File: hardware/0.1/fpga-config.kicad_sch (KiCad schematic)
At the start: 37 parts, among them J2 JTAG, J5 USB_C_Receptacle_USB2.0, Q1 BSS138, SW1 SW_Push, U1 ECP5U_12_CABGA256, U4 USBLC6-2SC6, U6 W25Q128JVSIQ

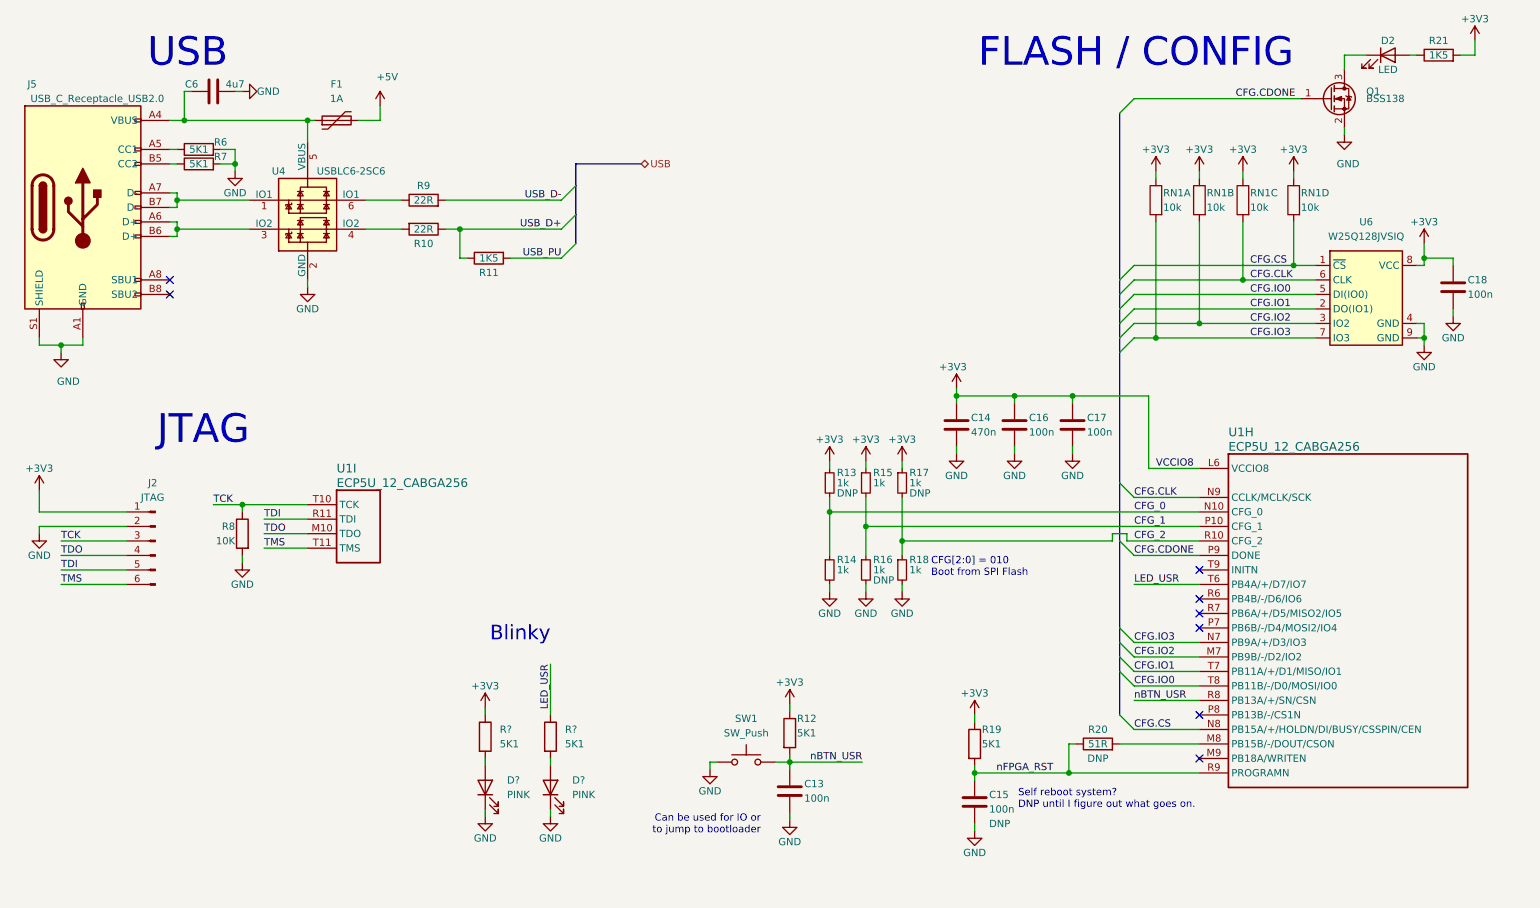
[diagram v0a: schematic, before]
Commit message: all 3d models added
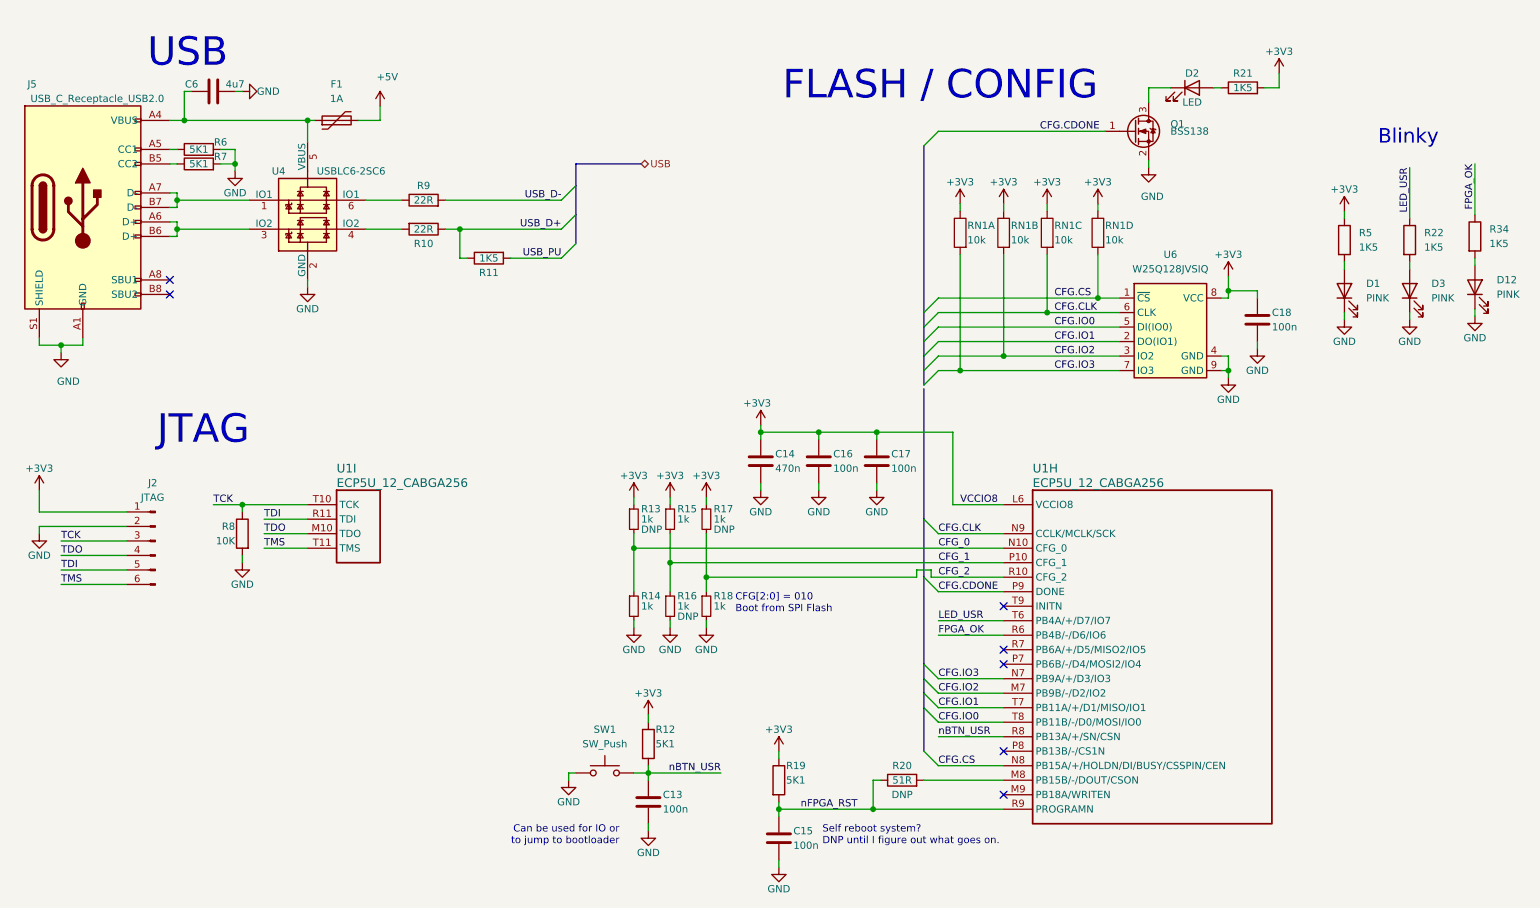
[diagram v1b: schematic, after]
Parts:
- added D12: PINK, LED_SMD:LED_0603_1608Metric, symbol Device:LED
- added R34: 1K5, Resistor_SMD:R_0402_1005Metric, symbol Device:R
- C15: DNP DNP -> (none)
- F1: footprint josh-passives-smt:Fuse_0805_2012Metric -> josh-passives-smt:Fuse_0603_1608Metric
- Q1: footprint Package_TO_SOT_SMD:SOT-23 -> Package_TO_SOT_SMD:SOT-323_SC-70
- R22, R5: renamed from R?; value 5K1 -> 1K5
- SW1: footprint josh-buttons-switches:SW_Push_PTS815 -> josh-buttons-switches:SW_Push_KMR2
- U6: footprint Package_SON:WSON-8-1EP_6x5mm_P1.27mm_EP3.4x4.3mm -> josh-soic-sot-etc:WSON-8-1EP_6x5mm_P1.27mm_EP3.4x4.3mm
- gave numbers to parts that had none: 2
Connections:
- net GND: now also D12.1 (K)
- net FPGA_OK: now reaches U1.R6 (PB4B/-/D6/IO6)
- net FPGA_OK: now also R34.1
- new net: D12.2 (A), R34.2
- no-connect marks 8 -> 7
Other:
- moved on the sheet: C13, C14, C15, C16, C17, C18, D1, D2, D3, Q1, R12, R13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

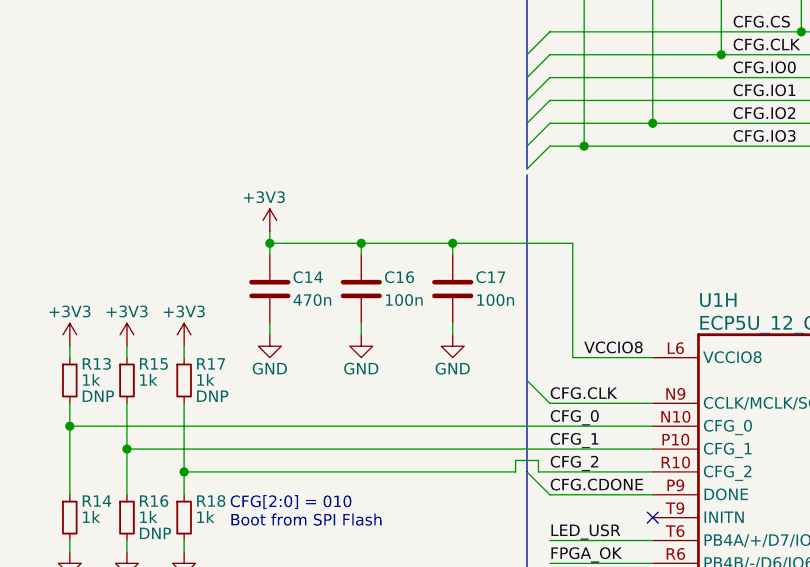
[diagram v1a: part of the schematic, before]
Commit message: decoupling down + outer pins fanned out
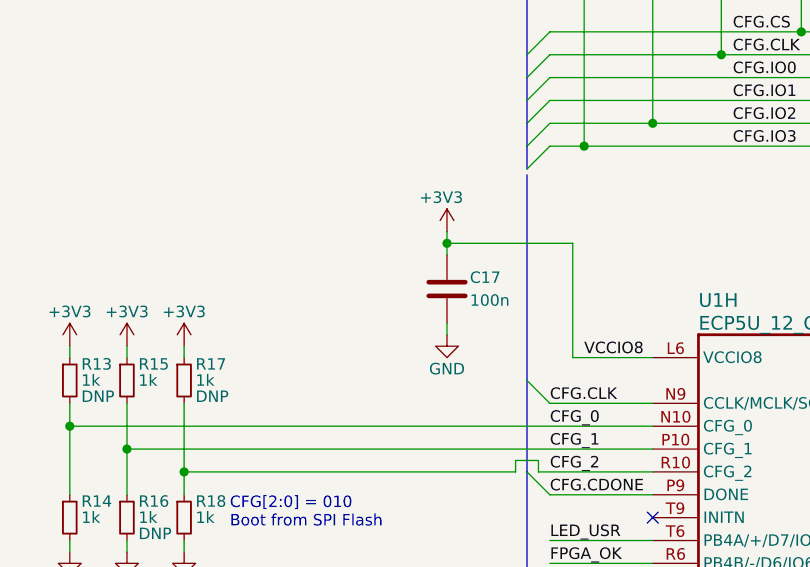
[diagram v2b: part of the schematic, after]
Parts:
- removed C14: 470n, Capacitor_SMD:C_0402_1005Metric, symbol Device:C
- removed C16: 100n, Capacitor_SMD:C_0402_1005Metric, symbol Device:C
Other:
- moved on the sheet: C17
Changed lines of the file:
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@@
   (junction (at 134.62 110.49) (diameter 1.016) (color 0 0 0 0))
   (junction (at 140.97 113.03) (diameter 1.016) (color 0 0 0 0))
-  (junction (at 150.495 87.63) (diameter 1.016) (color 0 0 0 0))
   (junction (at 153.67 153.67) (diameter 1.016) (color 0 0 0 0))
-  (junction (at 160.655 87.63) (diameter 1.016) (color 0 0 0 0))
+  (junction (at 170.18 87.63) (diameter 1.016) (color 0 0 0 0))
   (junction (at 170.18 153.67) (diameter 1.016) (color 0 0 0 0))
-  (junction (at 170.815 87.63) (diameter 1.016) (color 0 0 0 0))
   (junction (at 185.42 76.835) (diameter 1.016) (color 0 0 0 0))
   (junction (at 193.04 74.295) (diameter 1.016) (color 0 0 0 0))
@@
   (junction (at 232.41 62.865) (diameter 1.016) (color 0 0 0 0))
   (junction (at 232.41 76.835) (diameter 1.016) (color 0 0 0 0))
-  (no_connect (at 46.99 60.96))
-  (no_connect (at 193.04 143.51))
-  (no_connect (at 193.04 118.11))
-  (no_connect (at 46.99 63.5))
   (no_connect (at 193.04 125.73))
   (no_connect (at 193.04 128.27))
   (no_connect (at 193.04 151.13))
+  (no_connect (at 46.99 63.5))
+  (no_connect (at 193.04 118.11))
+  (no_connect (at 193.04 143.51))
+  (no_connect (at 46.99 60.96))
   (bus_entry (at 115.57 46.99) (size 2.54 -2.54)
     (stroke (width 0.1524) (type solid) (color 0 0 0 0))
@@
     (stroke (width 0) (type solid) (color 0 0 0 0))
   )
-  (wire (pts (xy 150.495 86.36) (xy 150.495 87.63))
-    (stroke (width 0) (type solid) (color 0 0 0 0))
-  )
-  (wire (pts (xy 150.495 87.63) (xy 150.495 88.9))
-    (stroke (width 0) (type solid) (color 0 0 0 0))
-  )
-  (wire (pts (xy 150.495 96.52) (xy 150.495 97.79))
-    (stroke (width 0) (type solid) (color 0 0 0 0))
-  )
   (wire (pts (xy 153.67 143.51) (xy 153.67 144.78))
     (stroke (width 0) (type solid) (color 0 0 0 0))
@@
     (stroke (width 0) (type solid) (color 0 0 0 0))
   )
-  (wire (pts (xy 160.655 87.63) (xy 150.495 87.63))
-    (stroke (width 0) (type solid) (color 0 0 0 0))
-  )
-  (wire (pts (xy 160.655 87.63) (xy 160.655 88.9))
-    (stroke (width 0) (type solid) (color 0 0 0 0))
-  )
-  (wire (pts (xy 160.655 87.63) (xy 170.815 87.63))
-    (stroke (width 0) (type solid) (color 0 0 0 0))
-  )
-  (wire (pts (xy 160.655 96.52) (xy 160.655 97.79))
+  (wire (pts (xy 170.18 86.36) (xy 170.18 87.63))
+    (stroke (width 0) (type solid) (color 0 0 0 0))
+  )
+  (wire (pts (xy 170.18 87.63) (xy 170.18 88.9))
+    (stroke (width 0) (type solid) (color 0 0 0 0))
+  )
+  (wire (pts (xy 170.18 87.63) (xy 184.15 87.63))
+    (stroke (width 0) (type solid) (color 0 0 0 0))
+  )
+  (wire (pts (xy 170.18 96.52) (xy 170.18 97.79))
     (stroke (width 0) (type solid) (color 0 0 0 0))
   )
@@
   )
   (wire (pts (xy 170.18 153.67) (xy 193.04 153.67))
-    (stroke (width 0) (type solid) (color 0 0 0 0))
-  )
-  (wire (pts (xy 170.815 87.63) (xy 170.815 88.9))
-    (stroke (width 0) (type solid) (color 0 0 0 0))
-  )
-  (wire (pts (xy 170.815 87.63) (xy 184.15 87.63))
-    (stroke (width 0) (type solid) (color 0 0 0 0))
-  )
-  (wire (pts (xy 170.815 96.52) (xy 170.815 97.79))
     (stroke (width 0) (type solid) (color 0 0 0 0))
   )
@@
     )
   )
-  (symbol (lib_id "power:+3V3") (at 150.495 86.36 0) (unit 1)
-    (in_bom yes) (on_board yes)
-    (property "Reference" "#PWR0141" (id 0) (at 150.495 90.17 0)
-      (effects (font (size 1.27 1.27)) hide)
-    )
-    (property "Value" "+3V3" (id 1) (at 149.86 82.55 0))
-    (property "Footprint" "" (id 2) (at 150.495 86.36 0)
-      (effects (font (size 1.27 1.27)) hide)
-    )
-    (property "Datasheet" "" (id 3) (at 150.495 86.36 0)
-      (effects (font (size 1.27 1.27)) hide)
-    )
-  )
   (symbol (lib_id "power:+3V3") (at 153.67 143.51 0) (unit 1)
     (in_bom yes) (on_board yes)
@@
     )
   )
+  (symbol (lib_id "power:+3V3") (at 170.18 86.36 0) (unit 1)
+    (in_bom yes) (on_board yes)
+    (property "Reference" "#PWR0141" (id 0) (at 170.18 90.17 0)
+      (effects (font (size 1.27 1.27)) hide)
+    )
+    (property "Value" "+3V3" (id 1) (at 169.545 82.55 0))
+    (property "Footprint" "" (id 2) (at 170.18 86.36 0)
+      (effects (font (size 1.27 1.27)) hide)
+    )
+    (property "Datasheet" "" (id 3) (at 170.18 86.36 0)
+      (effects (font (size 1.27 1.27)) hide)
+    )
+  )
   (symbol (lib_id "power:+3V3") (at 185.42 47.625 0) (unit 1)
     (in_bom yes) (on_board yes)
@@
     )
   )
-  (symbol (lib_id "power:GND") (at 150.495 97.79 0) (unit 1)
-    (in_bom yes) (on_board yes)
-    (property "Reference" "#PWR0142" (id 0) (at 150.495 104.14 0)
-      (effects (font (size 1.27 1.27)) hide)
-    )
-    (property "Value" "GND" (id 1) (at 150.495 101.6 0))
-    (property "Footprint" "" (id 2) (at 150.495 97.79 0)
-      (effects (font (size 1.27 1.27)) hide)
-    )
-    (property "Datasheet" "" (id 3) (at 150.495 97.79 0)
-      (effects (font (size 1.27 1.27)) hide)
-    )
-  )
   (symbol (lib_id "power:GND") (at 153.67 163.83 0) (unit 1)
     (in_bom yes) (on_board yes)
@@
     )
   )
-  (symbol (lib_id "power:GND") (at 160.655 97.79 0) (unit 1)
-    (in_bom yes) (on_board yes)
-    (property "Reference" "#PWR0143" (id 0) (at 160.655 104.14 0)
-      (effects (font (size 1.27 1.27)) hide)
-    )
-    (property "Value" "GND" (id 1) (at 160.655 101.6 0))
-    (property "Footprint" "" (id 2) (at 160.655 97.79 0)
-      (effects (font (size 1.27 1.27)) hide)
-    )
-    (property "Datasheet" "" (id 3) (at 160.655 97.79 0)
-      (effects (font (size 1.27 1.27)) hide)
-    )
-  )
-  (symbol (lib_id "power:GND") (at 170.815 97.79 0) (unit 1)
-    (in_bom yes) (on_board yes)
-    (property "Reference" "#PWR0140" (id 0) (at 170.815 104.14 0)
-      (effects (font (size 1.27 1.27)) hide)
-    )
-    (property "Value" "GND" (id 1) (at 170.815 101.6 0))
-    (property "Footprint" "" (id 2) (at 170.815 97.79 0)
-      (effects (font (size 1.27 1.27)) hide)
-    )
-    (property "Datasheet" "" (id 3) (at 170.815 97.79 0)
+  (symbol (lib_id "power:GND") (at 170.18 97.79 0) (unit 1)
+    (in_bom yes) (on_board yes)
+    (property "Reference" "#PWR0140" (id 0) (at 170.18 104.14 0)
+      (effects (font (size 1.27 1.27)) hide)
+    )
+    (property "Value" "GND" (id 1) (at 170.18 101.6 0))
+    (property "Footprint" "" (id 2) (at 170.18 97.79 0)
+      (effects (font (size 1.27 1.27)) hide)
+    )
+    (property "Datasheet" "" (id 3) (at 170.18 97.79 0)
       (effects (font (size 1.27 1.27)) hide)
     )
@@
     )
   )
-  (symbol (lib_id "Device:C") (at 150.495 92.71 0) (unit 1)
-    (in_bom yes) (on_board yes)
-    (property "Reference" "C14" (id 0) (at 153.035 91.44 0)
-      (effects (font (size 1.27 1.27)) (justify left))
-    )
-    (property "Value" "470n" (id 1) (at 153.035 93.98 0)
-      (effects (font (size 1.27 1.27)) (justify left))
-    )
-    (property "Footprint" "Capacitor_SMD:C_0402_1005Metric" (id 2) (at 151.4602 96.52 0)
-      (effects (font (size 1.27 1.27)) hide)
-    )
-    (property "Datasheet" "~" (id 3) (at 150.495 92.71 0)
-      (effects (font (size 1.27 1.27)) hide)
-    )
-  )
   (symbol (lib_id "Device:C") (at 153.67 158.75 0) (unit 1)
     (in_bom yes) (on_board yes)
@@
     )
   )
-  (symbol (lib_id "Device:C") (at 160.655 92.71 0) (unit 1)
-    (in_bom yes) (on_board yes)
-    (property "Reference" "C16" (id 0) (at 163.195 91.44 0)
-      (effects (font (size 1.27 1.27)) (justify left))
-    )
-    (property "Value" "100n" (id 1) (at 163.195 93.98 0)
-      (effects (font (size 1.27 1.27)) (justify left))
-    )
-    (property "Footprint" "Capacitor_SMD:C_0402_1005Metric" (id 2) (at 161.6202 96.52 0)
-      (effects (font (size 1.27 1.27)) hide)
-    )
-    (property "Datasheet" "~" (id 3) (at 160.655 92.71 0)
-      (effects (font (size 1.27 1.27)) hide)
-    )
-  )
-  (symbol (lib_id "Device:C") (at 170.815 92.71 0) (unit 1)
-    (in_bom yes) (on_board yes)
-    (property "Reference" "C17" (id 0) (at 173.355 91.44 0)
-      (effects (font (size 1.27 1.27)) (justify left))
-    )
-    (property "Value" "100n" (id 1) (at 173.355 93.98 0)
-      (effects (font (size 1.27 1.27)) (justify left))
-    )
-    (property "Footprint" "Capacitor_SMD:C_0402_1005Metric" (id 2) (at 171.7802 96.52 0)
-      (effects (font (size 1.27 1.27)) hide)
-    )
-    (property "Datasheet" "~" (id 3) (at 170.815 92.71 0)
-      (effects (font (size 1.27 1.27)) hide)
-    )
+  (symbol (lib_id "Device:C") (at 170.18 92.71 0) (unit 1)
+    (in_bom yes) (on_board yes)
+    (property "Reference" "C17" (id 0) (at 172.72 91.44 0)
+      (effects (font (size 1.27 1.27)) (justify left))
+    )
+    (property "Value" "100n" (id 1) (at 172.72 93.98 0)
+      (effects (font (size 1.27 1.27)) (justify left))
+    )
+    (property "Footprint" "Capacitor_SMD:C_0402_1005Metric" (id 2) (at 171.1452 96.52 0)
+      (effects (font (size 1.27 1.27)) hide)
+    )
+    (property "Datasheet" "~" (id 3) (at 170.18 92.71 0)
+      (effects (font (size 1.27 1.27)) hide)
+    )

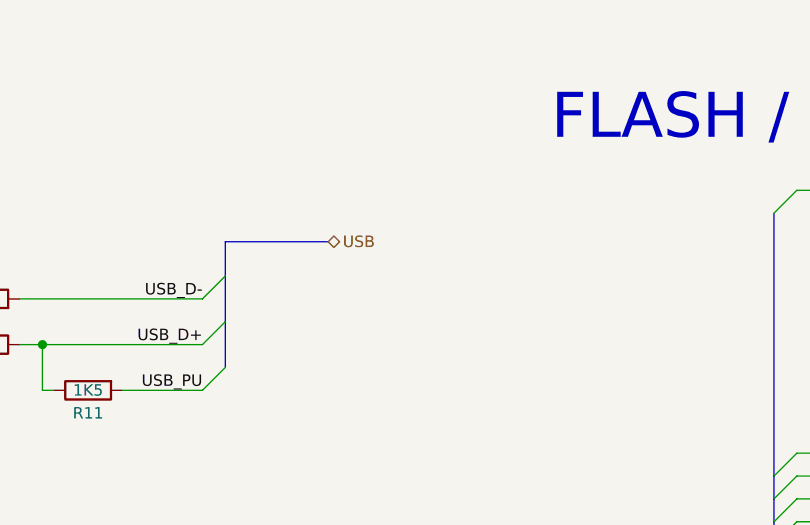
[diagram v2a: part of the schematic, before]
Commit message: cleaning up schematic
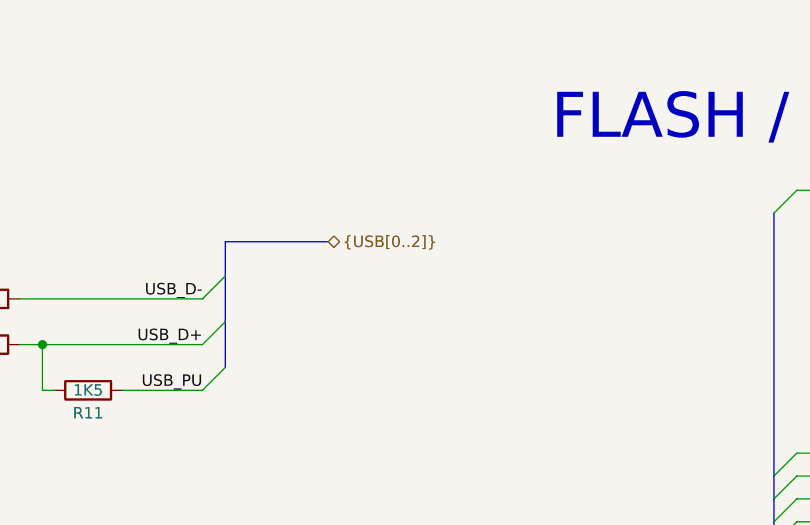
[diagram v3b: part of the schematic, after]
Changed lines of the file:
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@@
 (kicad_sch (version 20200820) (host eeschema "5.99.0-unknown-b0af66afc~103~ubuntu20.04.1")
-  (page 2 6)
+  (page 3 5)
   (paper "A4")
   (junction (at 27.94 72.39) (diameter 1.016) (color 0 0 0 0))
@@
   (junction (at 232.41 62.865) (diameter 1.016) (color 0 0 0 0))
   (junction (at 232.41 76.835) (diameter 1.016) (color 0 0 0 0))
+  (no_connect (at 193.04 151.13))
+  (no_connect (at 46.99 60.96))
+  (no_connect (at 193.04 118.11))
+  (no_connect (at 46.99 63.5))
+  (no_connect (at 193.04 143.51))
   (no_connect (at 193.04 125.73))
   (no_connect (at 193.04 128.27))
-  (no_connect (at 193.04 151.13))
-  (no_connect (at 46.99 63.5))
-  (no_connect (at 193.04 118.11))
-  (no_connect (at 193.04 143.51))
-  (no_connect (at 46.99 60.96))
   (bus_entry (at 115.57 46.99) (size 2.54 -2.54)
     (stroke (width 0.1524) (type solid) (color 0 0 0 0))
@@
     (effects (font (size 1.27 1.27)) (justify right bottom))
   )
-  (hierarchical_label "USB" (shape bidirectional) (at 129.54 40.64 0)
+  (hierarchical_label "{USB[0..2]}" (shape bidirectional) (at 129.54 40.64 0)
     (effects (font (size 1.27 1.27)) (justify left))
   )

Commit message: layout ++
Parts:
- R20: value 51R -> 22R
- RN1: value 10k -> 10K
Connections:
- net CFG.CLK: no longer RN1.2
- net CFG.IO1: now also RN1.2
- net LED_USR: now also U1.R7 (PB6A/+/D5/MISO2/IO5); no longer U1.T6 (PB4A/+/D7/IO7)
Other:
- moved on the sheet: C18, U6
